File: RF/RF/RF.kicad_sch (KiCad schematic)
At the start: 0 parts

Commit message: added external memory
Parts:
- added C101, C102, C103, C104: 220pF, Capacitor_SMD:C_0603_1608Metric_Pad1.08x0.95mm_HandSolder, symbol Device:C
- added FL101: SF2446E, SamacSys_Parts:SF2446E, symbol SamacSys_Parts:SF2446E
- added J101: Conn_Coaxial, Connector_Coaxial:SMA_Amphenol_901-143_Horizontal, symbol Connector:Conn_Coaxial
- added R101, R102, R103, R104, R105, R106, R107, R108, R109, R110, R111, R112, R113: 0R, Resistor_SMD:R_0603_1608Metric_Pad0.98x0.95mm_HandSolder, symbol Device:R
- added TP201: MOSI, TestPoint:TestPoint_Loop_D3.50mm_Drill1.4mm_Beaded, symbol Connector:TestPoint
- added TP201: MISO, TestPoint:TestPoint_Loop_D3.50mm_Drill1.4mm_Beaded, symbol Connector:TestPoint
- added TP201: CC_DC, TestPoint:TestPoint_Loop_D3.50mm_Drill1.4mm_Beaded, symbol Connector:TestPoint
- added TP201: SCK, TestPoint:TestPoint_Loop_D3.50mm_Drill1.4mm_Beaded, symbol Connector:TestPoint
- added TP201: CC_DD, TestPoint:TestPoint_Loop_D3.50mm_Drill1.4mm_Beaded, symbol Connector:TestPoint
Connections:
- new net: C104.2, J101.1 (In)
- new net Balun/CC_RF_N: R102.2
- new net Balun/CC_RF_P: R101.2
- new net Balun/UNBALANCED_RF: C101.1
- new net CC1110/AIN0: R107.1
- new net CC1110/CC_DC: TP201.1
- new net CC1110/CC_DD: TP201.1
- new net CC1110/CC_RF_N: R102.1
- new net CC1110/CC_RF_P: R101.1
- new net CC1110/LST_TX_MODE: R106.1
- new net CC1110/RF_BYP: R104.1
- new net CC1110/RF_EN: R105.1
- new net CC1110/UART0_CTS: R113.2
- new net CC1110/UART0_RTS: R111.2
- new net CC1110/UART0_RX: R112.2
- new net CC1110/UART0_TX: R110.2
- new net CC1110/~{FLASH_CS}: R109.1
- new net CC1110/~{LST_RX_MODE}: R103.1
- new net CC1110/~{SRAM_CS}: R108.1
- new net Connectors/UART0_CTS: R113.1
- new net Connectors/UART0_RTS: R111.1
- new net Connectors/UART0_RX: R112.1
- new net Connectors/UART0_TX: R110.1
- new net External Memory/~{FRAM_CS}: R109.2
- new net External Memory/~{SRAM_CS}: R108.2
- new net GND: FL101.1 (GND_1), FL101.3 (GND_2), FL101.4 (GND_3), FL101.6 (GND_4), J101.2 (Ext)
- new net MISO: TP201.1
- new net MOSI: TP201.1
- new net RF Front End/ANTENNA: C104.1
- new net RF Front End/LST_TX_MODE: R106.2
- new net RF Front End/PA_VAPC: R107.2
- new net RF Front End/RF_BYP: R104.2
- new net RF Front End/RF_EN: R105.2
- new net RF Front End/RX: C102.2
- new net RF Front End/SAW1: FL101.5 (OUTPUT)
- new net RF Front End/SAW2: FL101.2 (INPUT)
- new net RF Front End/TX: C103.2
- new net RF Switch/RX: C102.1
- new net RF Switch/TX: C103.1
- new net RF Switch/UNBALANCED_RF: C101.2
- new net RF Switch/~{LST_RX_MODE}: R103.2
- new net SCK: TP201.1
- no-connect marks 0 -> 5
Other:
- added sheet External Memory (memory.kicad_sch)
- sheet Balun ports: added CC_RF_N, CC_RF_P, UNBALANCED_RF; removed none
- sheet CC1110 ports: added AIN0, CC_DC, CC_DD, CC_RF_N, CC_RF_P, LST_TX_MODE, MISO, MOSI, RF_BYP, RF_EN, SCK, UART0_CTS, UART0_RTS, UART0_RX, UART0_TX, ~{FLASH_CS}, ~{LST_RX_MODE}, ~{SRAM_CS}; removed none
- sheet Connectors ports: added CC_DC, CC_DD, CC_SPI_MISO, CC_SPI_MOSI, CC_SPI_SCK, UART0_CTS, UART0_RTS, UART0_RX, UART0_TX, ~{CC_SPI_SSN}, ~{RESET}; removed none
- sheet RF Front End ports: added ANTENNA, LST_TX_MODE, PA_VAPC, RF_BYP, RF_EN, RX, SAW1, SAW2, TX; removed none
- sheet RF Switch ports: added RX, TX, UNBALANCED_RF, ~{LST_RX_MODE}; removed none
- note added: "Antenna"
- note added: "OR resistors also act as test points"
- note added: "Route as 50 ohms"
- note added: "SAW FILTER"

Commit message: RF: Push for schematic capture review version 1.0
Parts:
- added H101, H102, H103, H104: MountingHole_Pad, MountingHole:MountingHole_2.2mm_M2_DIN965_Pad, symbol Mechanical:MountingHole_Pad
- added R114, R115, R116, R117: DNP, Resistor_SMD:R_0603_1608Metric_Pad0.98x0.95mm_HandSolder, symbol Device:R
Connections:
- net GND: now also R114.1, R115.1, R116.1, R117.1
- net External Memory/~{FRAM_CS} renamed External Memory/~{FLASH_CS}
- new net: H101.1, R114.2
- new net: H103.1, R116.2
- new net: H102.1, R115.2
- new net: H104.1, R117.2
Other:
- sheet External Memory ports: added ~{FLASH_CS}; removed ~{FRAM_CS}
- note added: "MOUNTING HOLES"
- moved on the sheet: TP201

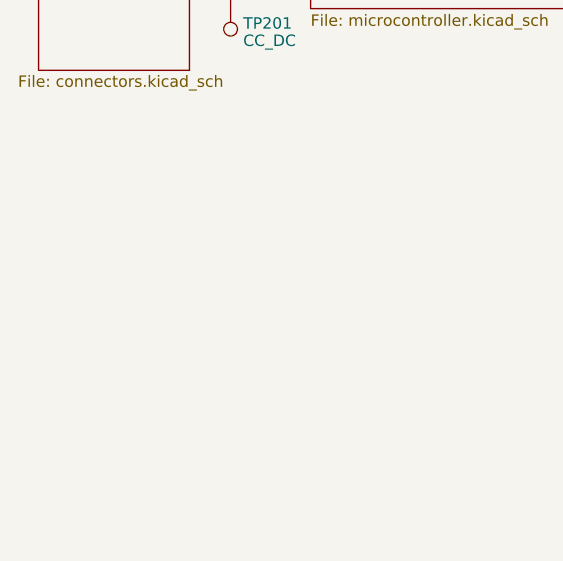
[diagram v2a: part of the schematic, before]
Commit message: added standard connector and some initial layout
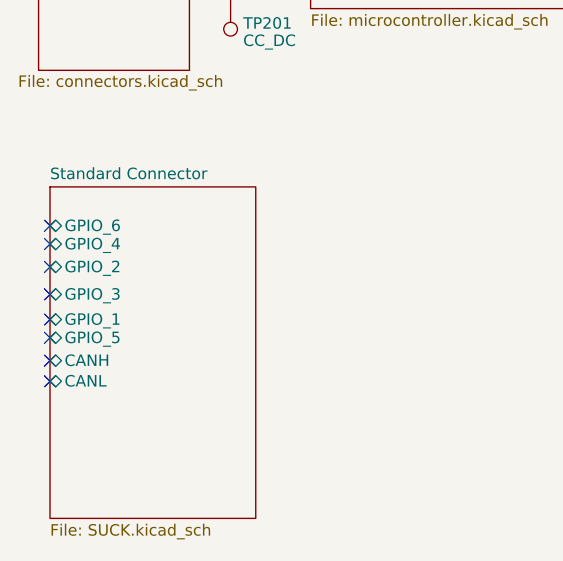
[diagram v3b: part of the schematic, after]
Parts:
- H101, H102, H103, H104: footprint MountingHole:MountingHole_2.2mm_M2_DIN965_Pad -> MountingHole:MountingHole_3mm_Pad
- J101: footprint Connector_Coaxial:SMA_Amphenol_901-143_Horizontal -> Connector_Coaxial:SMA_Amphenol_132289_EdgeMount
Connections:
- no-connect marks 5 -> 13
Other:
- added sheet Standard Connector (SUCK.kicad_sch)
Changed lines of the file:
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@@
   )
   (no_connect (at 32.512 27.94))
+  (no_connect (at 17.018 168.91))
+  (no_connect (at 17.018 159.258))
+  (no_connect (at 17.018 162.052))
+  (no_connect (at 17.018 153.67))
+  (no_connect (at 17.018 164.084))
   (no_connect (at 32.512 35.56))
   (no_connect (at 32.512 33.02))
+  (no_connect (at 17.018 156.21))
   (no_connect (at 32.512 25.654))
+  (no_connect (at 17.018 151.638))
+  (no_connect (at 17.018 166.624))
   (no_connect (at 32.512 30.226))
   (wire (pts (xy 41.148 88.392) (xy 45.974 88.392))
@@
       (effects (font (size 1.27 1.27)) (justify left))
     )
-    (property "Footprint" "Connector_Coaxial:SMA_Amphenol_901-143_Horizontal" (at 257.81 75.184 0)
+    (property "Footprint" "Connector_Coaxial:SMA_Amphenol_132289_EdgeMount" (at 257.81 75.184 0)
       (effects (font (size 1.27 1.27)) hide)
     )
@@
       (effects (font (size 1.27 1.27)) (justify left))
     )
-    (property "Footprint" "MountingHole:MountingHole_2.2mm_M2_DIN965_Pad" (at 130.81 163.322 0)
+    (property "Footprint" "MountingHole:MountingHole_3mm_Pad" (at 130.81 163.322 0)
       (effects (font (size 1.27 1.27)) hide)
     )
@@
       (effects (font (size 1.27 1.27)) (justify left))
     )
-    (property "Footprint" "MountingHole:MountingHole_2.2mm_M2_DIN965_Pad" (at 130.302 151.638 0)
+    (property "Footprint" "MountingHole:MountingHole_3mm_Pad" (at 130.302 151.638 0)
       (effects (font (size 1.27 1.27)) hide)
     )
@@
       (effects (font (size 1.27 1.27)) (justify left))
     )
-    (property "Footprint" "MountingHole:MountingHole_2.2mm_M2_DIN965_Pad" (at 130.556 157.48 0)
+    (property "Footprint" "MountingHole:MountingHole_3mm_Pad" (at 130.556 157.48 0)
       (effects (font (size 1.27 1.27)) hide)
     )
@@
       (effects (font (size 1.27 1.27)) (justify left))
     )
-    (property "Footprint" "MountingHole:MountingHole_2.2mm_M2_DIN965_Pad" (at 131.064 169.418 0)
+    (property "Footprint" "MountingHole:MountingHole_3mm_Pad" (at 131.064 169.418 0)
       (effects (font (size 1.27 1.27)) hide)
     )
@@
       )
     )
+  )
+  (sheet (at 17.018 147.32) (size 22.86 36.83) (fields_autoplaced)
+    (stroke (width 0.1524) (type solid))
+    (fill (color 169 220 255 1.0000))
+    (property "Sheetname" "Standard Connector" (at 17.018 146.6084 0)
+      (effects (font (size 1.27 1.27)) (justify left bottom))
+    )
+    (property "Sheetfile" "SUCK.kicad_sch" (at 17.018 184.7346 0)
+      (effects (font (size 1.27 1.27)) (justify left top))
+    )
+    (pin "GPIO_4" bidirectional (at 17.018 153.67 180)
+      (effects (font (size 1.27 1.27)) (justify left))
+    )
+    (pin "GPIO_2" bidirectional (at 17.018 156.21 180)
+      (effects (font (size 1.27 1.27)) (justify left))
+    )
+    (pin "GPIO_3" bidirectional (at 17.018 159.258 180)
+      (effects (font (size 1.27 1.27)) (justify left))
+    )
+    (pin "GPIO_1" bidirectional (at 17.018 162.052 180)
+      (effects (font (size 1.27 1.27)) (justify left))
+    )
+    (pin "GPIO_5" bidirectional (at 17.018 164.084 180)
+      (effects (font (size 1.27 1.27)) (justify left))
+    )
+    (pin "CANH" bidirectional (at 17.018 166.624 180)
+      (effects (font (size 1.27 1.27)) (justify left))
+    )
+    (pin "CANL" bidirectional (at 17.018 168.91 180)
+      (effects (font (size 1.27 1.27)) (justify left))
+    )
+    (pin "GPIO_6" bidirectional (at 17.018 151.638 180)
+      (effects (font (size 1.27 1.27)) (justify left))
+    )
+    (instances
+      (project "RF"
+        (path "/51251c4d-d12e-4de3-8dd9-04d485d7d417" (page "8"))
+      )
+    )

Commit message: layout rev 1.0
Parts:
- removed R110, R111, R112, R113: 0R, Resistor_SMD:R_0603_1608Metric_Pad0.98x0.95mm_HandSolder, symbol Device:R
- TP201: footprint TestPoint:TestPoint_Loop_D3.50mm_Drill1.4mm_Beaded -> TestPoint:TestPoint_THTPad_1.0x1.0mm_Drill0.5mm

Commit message: connections ting
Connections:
- net RF Front End/ANTENNA: now also C104.2; no longer C104.1
- net at J101.1 (In): now also C104.1; no longer C104.2
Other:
- moved on the sheet: C104
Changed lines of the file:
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@@
     )
   )
-  (symbol (lib_id "Device:C") (at 245.11 75.184 90) (unit 1)
-    (in_bom yes) (on_board yes) (dnp no) (fields_autoplaced)
+  (symbol (lib_id "Device:C") (at 245.11 75.184 270) (mirror x) (unit 1)
+    (in_bom yes) (on_board yes) (dnp no)
     (property "Reference" "C104" (at 245.11 70.0151 90)
       (effects (font (size 1.27 1.27)))
@@
       (effects (font (size 1.27 1.27)))
     )
-    (property "Footprint" "Capacitor_SMD:C_0603_1608Metric_Pad1.08x0.95mm_HandSolder" (at 248.92 74.2188 0)
+    (property "Footprint" "Capacitor_SMD:C_0603_1608Metric_Pad1.08x0.95mm_HandSolder" (at 241.3 74.2188 0)
       (effects (font (size 1.27 1.27)) hide)
     )
